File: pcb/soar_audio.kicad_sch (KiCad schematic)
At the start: 101 parts, among them J1 RJ45-FLAPS, J2 RJ12-FLAPS, J3 HEADER_4, J4 Screw_Terminal_01x02, J5 RJ45-CAN, J6 HEADER_4, Q1 AO3401A, U1 LV2842X, U3 SN65HVD231, U4 PAM8302AAS, U6 BP

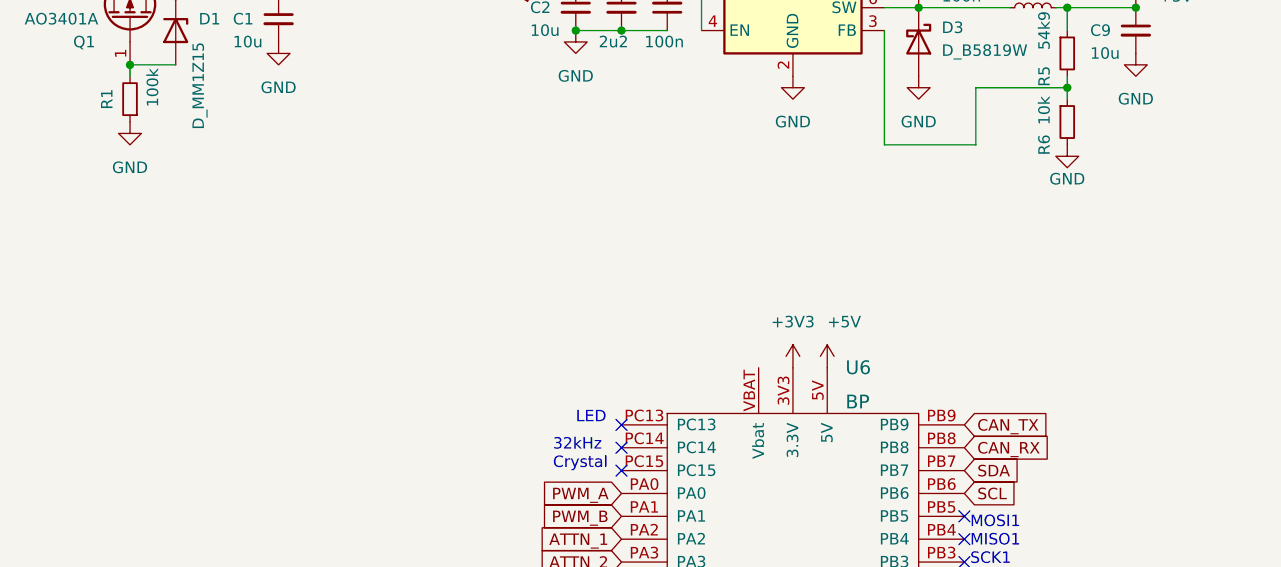
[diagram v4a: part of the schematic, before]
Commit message: updated jlc rules to layout
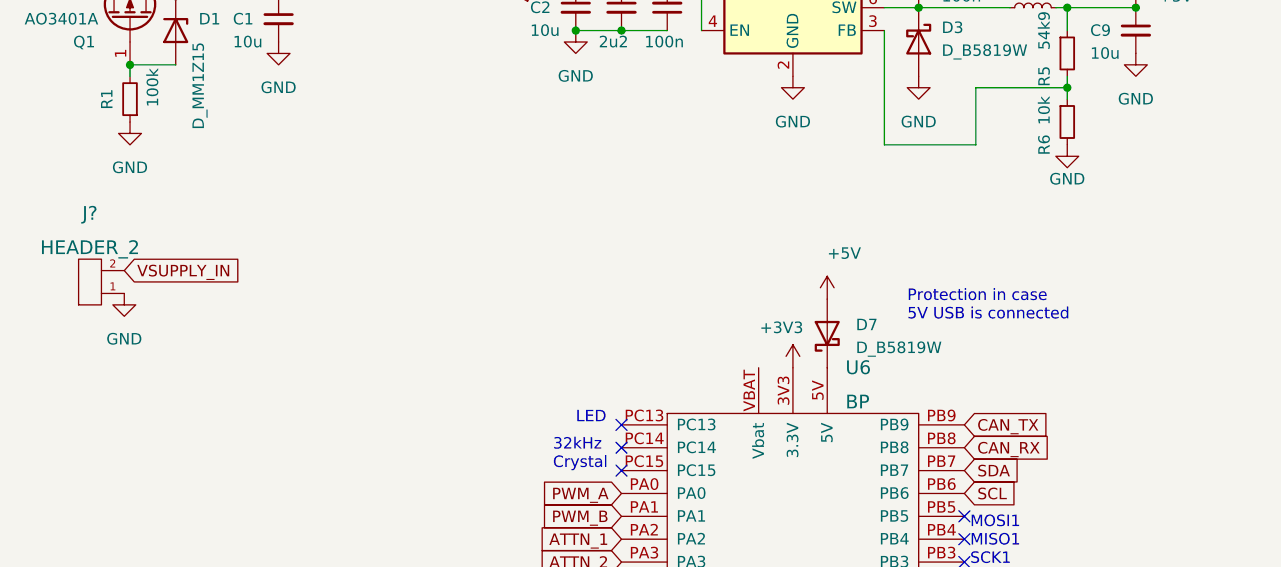
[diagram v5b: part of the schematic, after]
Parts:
- added D7: D_B5819W, Diode_SMD:D_SOD-123, symbol Device:D_Schottky
- added J?: HEADER_2, Connector_PinHeader_1.27mm:PinHeader_1x02_P1.27mm_Vertical, symbol STM32F4Di:HEADER_2
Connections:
- net +5V: now also D7.2 (A); no longer U6.5V
- net GND: now also J?.1
- net VSUPPLY_IN: now also J?.2
- new net: D7.1 (K), U6.5V
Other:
- note added: "Protection in case 5V USB is connected"
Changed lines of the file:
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@@
     (stroke (width 0) (type default) (color 0 0 0 0))
   )
+  (text "Protection in case \n5V USB is connected " (at 110.49 62.865 0)
+    (effects (font (size 1.27 1.27)) (justify left bottom))
+  )
   (text "Micro\nUSB" (at 118.11 97.155 0)
     (effects (font (size 1.27 1.27)) (justify left bottom))
@@
     )
   )
+  (global_label "VSUPPLY_IN" (shape input) (at 23.495 57.15 0) (fields_autoplaced)
+    (effects (font (size 1.27 1.27)) (justify left))
+    (property "Intersheet References" "${INTERSHEET_REFS}" (id 0) (at 37.0962 57.0706 0)
+      (effects (font (size 1.27 1.27)) (justify left) hide)
+    )
+  )
   (global_label "PWM_B" (shape input) (at 78.74 84.455 180) (fields_autoplaced)
     (effects (font (size 1.27 1.27)) (justify right))
@@
     (pin "1")
   )
-  (symbol (lib_id "power:+5V") (at 101.6 67.945 0) (unit 1)
+  (symbol (lib_id "power:+5V") (at 101.6 60.325 0) (unit 1)
     (in_bom yes) (on_board yes)
-    (property "Reference" "#PWR0106" (id 0) (at 101.6 71.755 0)
+    (property "Reference" "#PWR0106" (id 0) (at 101.6 64.135 0)
       (effects (font (size 1.27 1.27)) hide)
     )
-    (property "Value" "+5V" (id 1) (at 101.6 62.865 0)
+    (property "Value" "+5V" (id 1) (at 101.6 55.245 0)
       (effects (font (size 1.27 1.27)) (justify left))
     )
-    (property "Footprint" "" (id 2) (at 101.6 67.945 0)
+    (property "Footprint" "" (id 2) (at 101.6 60.325 0)
       (effects (font (size 1.27 1.27)) hide)
     )
-    (property "Datasheet" "" (id 3) (at 101.6 67.945 0)
+    (property "Datasheet" "" (id 3) (at 101.6 60.325 0)
       (effects (font (size 1.27 1.27)) hide)
     )
@@
     (pin "1")
   )
+  (symbol (lib_id "STM32F4Di:HEADER_2") (at 20.955 58.42 180) (unit 1)
+    (in_bom yes) (on_board yes) (fields_autoplaced)
+    (property "Reference" "J?" (id 0) (at 19.685 50.8 0)
+      (effects (font (size 1.524 1.524)))
+    )
+    (property "Value" "HEADER_2" (id 1) (at 19.685 54.61 0)
+      (effects (font (size 1.524 1.524)))
+    )
+    (property "Footprint" "Connector_PinHeader_1.27mm:PinHeader_1x02_P1.27mm_Vertical" (id 2) (at 20.955 58.42 0)
+      (effects (font (size 1.524 1.524)) hide)
+    )
+    (property "Datasheet" "" (id 3) (at 20.955 58.42 0)
+      (effects (font (size 1.524 1.524)))
+    )
+    (pin "1")
+    (pin "2")
+  )
   (symbol (lib_id "Jumper:SolderJumper_2_Bridged") (at 289.56 41.91 0) (unit 1)
     (in_bom yes) (on_board yes) (fields_autoplaced)
@@
   )
   (symbol (lib_id "power:+3V3") (at 97.79 67.945 0) (unit 1)
-    (in_bom yes) (on_board yes) (fields_autoplaced)
+    (in_bom yes) (on_board yes)
     (property "Reference" "#PWR0103" (id 0) (at 97.79 71.755 0)
       (effects (font (size 1.27 1.27)) hide)
     )
-    (property "Value" "+3V3" (id 1) (at 97.79 62.865 0))
+    (property "Value" "+3V3" (id 1) (at 96.52 63.5 0))
     (property "Footprint" "" (id 2) (at 97.79 67.945 0)
       (effects (font (size 1.27 1.27)) hide)
@@
     (pin "2")
   )
+  (symbol (lib_id "Device:D_Schottky") (at 101.6 64.135 90) (unit 1)
+    (in_bom yes) (on_board yes) (fields_autoplaced)
+    (property "Reference" "D7" (id 0) (at 104.775 63.1824 90)
+      (effects (font (size 1.27 1.27)) (justify right))
+    )
+    (property "Value" "D_B5819W" (id 1) (at 104.775 65.7224 90)
+      (effects (font (size 1.27 1.27)) (justify right))
+    )
+    (property "Footprint" "Diode_SMD:D_SOD-123" (id 2) (at 101.6 64.135 0)
+      (effects (font (size 1.27 1.27)) hide)
+    )
+    (property "Datasheet" "~" (id 3) (at 101.6 64.135 0)
+      (effects (font (size 1.27 1.27)) hide)
+    )
+    (property "LCSC" "C8598" (id 4) (at 101.6 64.135 0)
+      (effects (font (size 1.27 1.27)) hide)
+    )
+    (pin "1")
+    (pin "2")
+  )
   (symbol (lib_id "power:GND") (at 208.28 271.78 0) (unit 1)
     (in_bom yes) (on_board yes) (fields_autoplaced)
@@
     (pin "1")
   )
+  (symbol (lib_id "power:GND") (at 23.495 59.69 0) (unit 1)
+    (in_bom yes) (on_board yes) (fields_autoplaced)
+    (property "Reference" "#PWR?" (id 0) (at 23.495 66.04 0)
+      (effects (font (size 1.27 1.27)) hide)
+    )
+    (property "Value" "GND" (id 1) (at 23.495 64.77 0))
+    (property "Footprint" "" (id 2) (at 23.495 59.69 0)
+      (effects (font (size 1.27 1.27)) hide)
+    )
+    (property "Datasheet" "" (id 3) (at 23.495 59.69 0)
+      (effects (font (size 1.27 1.27)) hide)
+    )
+    (pin "1")
+  )
   (symbol (lib_id "power:GND") (at 368.3 229.87 0) (unit 1)
     (in_bom yes) (on_board yes) (fields_autoplaced)
@@
       (reference "#PWR0171") (unit 1) (value "GND") (footprint "")
     )
+    (path "/c647da41-dec5-4eb3-8500-b17805fb64eb"
+      (reference "#PWR?") (unit 1) (value "GND") (footprint "")
+    )
     (path "/a51bbaf4-f7d2-4a58-a4c1-5ed98eb88444"
       (reference "C1") (unit 1) (value "10u") (footprint "Capacitor_SMD:C_0805_2012Metric")
@@
       (reference "D6") (unit 1) (value "D_TVS") (footprint "Diode_SMD:D_SOD-323")
     )
+    (path "/8bb69c77-9bde-4b48-a56c-65e3612a0972"
+      (reference "D7") (unit 1) (value "D_B5819W") (footprint "Diode_SMD:D_SOD-123")
+    )
     (path "/efe4d98c-f6d4-4c90-8c2f-cc9439fcf12d"
       (reference "D12") (unit 1) (value "D_TVS") (footprint "Diode_SMD:D_SOD-323")
@@
       (reference "J6") (unit 1) (value "HEADER_4") (footprint "Connector_PinHeader_1.27mm:PinHeader_1x04_P1.27mm_Vertical")
     )
+    (path "/3fb03f90-3fec-4ac2-b7dd-c48a6f5bb639"
+      (reference "J?") (unit 1) (value "HEADER_2") (footprint "Connector_PinHeader_1.27mm:PinHeader_1x02_P1.27mm_Vertical")
+    )
     (path "/4092c484-f701-46a1-a6e8-1f78398b9d7b"

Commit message: some more steps done
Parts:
- gave numbers to parts that had none: 1
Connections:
- net +3V3: now also U6.VBAT (Vbat)
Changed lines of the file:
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@@
   (junction (at 252.73 41.91) (diameter 0) (color 0 0 0 0)
   )
+  (junction (at 132.08 27.94) (diameter 0) (color 0 0 0 0)
+  )
   (junction (at 86.36 266.7) (diameter 0) (color 0 0 0 0)
   )
@@
     (stroke (width 0) (type default) (color 0 0 0 0))
   )
+  (wire (pts (xy 29.21 26.67) (xy 40.64 26.67))
+    (stroke (width 0) (type default) (color 0 0 0 0))
+  )
   (wire (pts (xy 198.12 266.7) (xy 200.66 266.7))
     (stroke (width 0) (type default) (color 0 0 0 0))
@@
     (stroke (width 0) (type default) (color 0 0 0 0))
   )
-  (wire (pts (xy 29.21 26.67) (xy 40.64 26.67))
-    (stroke (width 0) (type default) (color 0 0 0 0))
-  )
   (wire (pts (xy 325.12 29.21) (xy 325.12 43.18))
     (stroke (width 0) (type default) (color 0 0 0 0))
@@
     (stroke (width 0) (type default) (color 0 0 0 0))
   )
+  (wire (pts (xy 132.08 27.94) (xy 135.89 27.94))
+    (stroke (width 0) (type default) (color 0 0 0 0))
+  )
   (wire (pts (xy 293.37 41.91) (xy 295.91 41.91))
     (stroke (width 0) (type default) (color 0 0 0 0))
@@
     (stroke (width 0) (type default) (color 0 0 0 0))
   )
-  (wire (pts (xy 128.27 27.94) (xy 135.89 27.94))
+  (wire (pts (xy 128.27 27.94) (xy 132.08 27.94))
     (stroke (width 0) (type default) (color 0 0 0 0))
   )
@@
     (effects (font (size 1.27 1.27)) (justify right bottom))
   )
-  (text "Reverse polarity \nprotection" (at 22.86 21.59 0)
+  (text "Reverse polarity \nprotection" (at 22.86 19.685 0)
     (effects (font (size 1.27 1.27)) (justify left bottom))
   )
@@
     (pin "2")
   )
+  (symbol (lib_id "power:+3V3") (at 93.98 67.945 0) (unit 1)
+    (in_bom yes) (on_board yes)
+    (property "Reference" "#PWR0123" (id 0) (at 93.98 71.755 0)
+      (effects (font (size 1.27 1.27)) hide)
+    )
+    (property "Value" "+3V3" (id 1) (at 90.805 62.865 0))
+    (property "Footprint" "" (id 2) (at 93.98 67.945 0)
+      (effects (font (size 1.27 1.27)) hide)
+    )
+    (property "Datasheet" "" (id 3) (at 93.98 67.945 0)
+      (effects (font (size 1.27 1.27)) hide)
+    )
+    (pin "1")
+  )
   (symbol (lib_id "power:GND") (at 40.64 31.75 0) (unit 1)
     (in_bom yes) (on_board yes) (fields_autoplaced)
@@
   (symbol (lib_id "STM32F4Di:HEADER_2") (at 20.955 58.42 180) (unit 1)
     (in_bom yes) (on_board yes) (fields_autoplaced)
-    (property "Reference" "J?" (id 0) (at 19.685 50.8 0)
+    (property "Reference" "J7" (id 0) (at 19.685 50.8 0)
       (effects (font (size 1.524 1.524)))
     )
@@
   (symbol (lib_id "power:GND") (at 23.495 59.69 0) (unit 1)
     (in_bom yes) (on_board yes) (fields_autoplaced)
-    (property "Reference" "#PWR?" (id 0) (at 23.495 66.04 0)
+    (property "Reference" "#PWR0122" (id 0) (at 23.495 66.04 0)
       (effects (font (size 1.27 1.27)) hide)
     )
@@
     (pin "1")
   )
+  (symbol (lib_id "power:PWR_FLAG") (at 87.63 25.4 0) (unit 1)
+    (in_bom yes) (on_board yes) (fields_autoplaced)
+    (property "Reference" "#FLG0101" (id 0) (at 87.63 23.495 0)
+      (effects (font (size 1.27 1.27)) hide)
+    )
+    (property "Value" "PWR_FLAG" (id 1) (at 87.63 20.32 0))
+    (property "Footprint" "" (id 2) (at 87.63 25.4 0)
+      (effects (font (size 1.27 1.27)) hide)
+    )
+    (property "Datasheet" "~" (id 3) (at 87.63 25.4 0)
+      (effects (font (size 1.27 1.27)) hide)
+    )
+    (pin "1")
+  )
   (symbol (lib_id "Device:R_Small") (at 128.27 33.02 0) (unit 1)
     (in_bom yes) (on_board yes)
@@
     (pin "8")
   )
+  (symbol (lib_id "power:PWR_FLAG") (at 132.08 27.94 0) (unit 1)
+    (in_bom yes) (on_board yes) (fields_autoplaced)
+    (property "Reference" "#FLG0102" (id 0) (at 132.08 26.035 0)
+      (effects (font (size 1.27 1.27)) hide)
+    )
+    (property "Value" "PWR_FLAG" (id 1) (at 132.08 22.86 0))
+    (property "Footprint" "" (id 2) (at 132.08 27.94 0)
+      (effects (font (size 1.27 1.27)) hide)
+    )
+    (property "Datasheet" "~" (id 3) (at 132.08 27.94 0)
+      (effects (font (size 1.27 1.27)) hide)
+    )
+    (pin "1")
+  )
   (symbol (lib_id "Device:R_Small") (at 91.44 266.7 90) (unit 1)
     (in_bom yes) (on_board yes)
@@
   )
   (symbol_instances
+    (path "/c708a8f7-5414-4765-825a-e9983973a42f"
+      (reference "#FLG0101") (unit 1) (value "PWR_FLAG") (footprint "")
+    )
+    (path "/db3c9c99-6db5-4aed-a2c4-054e13bea135"
+      (reference "#FLG0102") (unit 1) (value "PWR_FLAG") (footprint "")
+    )
     (path "/77097033-ef67-4935-8349-94e2120bba17"
       (reference "#PWR0101") (unit 1) (value "GND") (footprint "")
@@
       (reference "#PWR0121") (unit 1) (value "+3V3") (footprint "")
     )
+    (path "/c647da41-dec5-4eb3-8500-b17805fb64eb"
+      (reference "#PWR0122") (unit 1) (value "GND") (footprint "")
+    )
+    (path "/06778dcf-032d-45a6-a8a1-a1bf5504a70d"
+      (reference "#PWR0123") (unit 1) (value "+3V3") (footprint "")
+    )
     (path "/3c85ce09-cd75-4b87-b41d-0c94ea5ee712"
       (reference "#PWR0124") (unit 1) (value "+5V") (footprint "")
@@
       (reference "#PWR0171") (unit 1) (value "GND") (footprint "")
     )
-    (path "/c647da41-dec5-4eb3-8500-b17805fb64eb"
-      (reference "#PWR?") (unit 1) (value "GND") (footprint "")
-    )
     (path "/a51bbaf4-f7d2-4a58-a4c1-5ed98eb88444"
       (reference "C1") (unit 1) (value "10u") (footprint "Capacitor_SMD:C_0805_2012Metric")
@@
     )
     (path "/3fb03f90-3fec-4ac2-b7dd-c48a6f5bb639"
-      (reference "J?") (unit 1) (value "HEADER_2") (footprint "Connector_PinHeader_1.27mm:PinHeader_1x02_P1.27mm_Vertical")
+      (reference "J7") (unit 1) (value "HEADER_2") (footprint "Connector_PinHeader_1.27mm:PinHeader_1x02_P1.27mm_Vertical")
     )
     (path "/4092c484-f701-46a1-a6e8-1f78398b9d7b"

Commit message: add toolingholes
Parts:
- added C10: 100n, Capacitor_SMD:C_0603_1608Metric, symbol Device:C_Small
- added C8: 1u, Capacitor_SMD:C_0603_1608Metric, symbol Device:C_Small
- added J8, J9: HEADER_4, Connector_PinHeader_2.54mm:PinHeader_1x04_P2.54mm_Vertical, symbol STM32F4Di:HEADER_4
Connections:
- net +3V3: now also J2.6, J9.3, J9.4; no longer J2.1
- net +5V: now also C10.2, C8.1, J8.3, J8.4
- net Flaps_Input1: now also J1.8; no longer J1.1
- net GND: now also J1.1, J2.1, J5.1, J5.2, C10.1, C8.2, J8.1, J8.2, J9.1, J9.2; no longer J1.8, J2.6, J5.7, J5.8
- net VSUPPLY_IN: now also J5.7, J5.8; no longer J5.1, J5.2
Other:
- note removed: "3V3 + GND + 5 Ausgänge 16LEDs"

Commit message: replaced out of stock inductor
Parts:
- L1: footprint Inductor_SMD:L_Bourns-SRN4018 -> OWN_PARTS:MWSA0402S; LCSC C98402 -> C408339
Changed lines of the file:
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@@
     (property "Reference" "L1" (id 0) (at 124.46 22.86 90))
     (property "Value" "10u" (id 1) (at 124.46 25.4 90))
-    (property "Footprint" "Inductor_SMD:L_Bourns-SRN4018" (id 2) (at 124.46 27.94 0)
+    (property "Footprint" "OWN_PARTS:MWSA0402S" (id 2) (at 124.46 27.94 0)
       (effects (font (size 1.27 1.27)) hide)
     )
@@
       (effects (font (size 1.27 1.27)) hide)
     )
-    (property "LCSC" "C98402" (id 4) (at 124.46 27.94 0)
+    (property "LCSC" "C408339" (id 4) (at 124.46 27.94 0)
       (effects (font (size 1.27 1.27)) hide)
     )
@@
     )
     (path "/bcf1cadf-0e3c-4d47-a1a1-9c7972c188f6"
-      (reference "L1") (unit 1) (value "10u") (footprint "Inductor_SMD:L_Bourns-SRN4018")
+      (reference "L1") (unit 1) (value "10u") (footprint "OWN_PARTS:MWSA0402S")
     )
     (path "/6f92a4e0-547a-4aa5-a7ae-7bdd5317a4f1"
